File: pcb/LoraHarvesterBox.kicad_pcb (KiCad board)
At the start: 4 copper layers, 48 x 45.5 mm, 45 parts, among them J1 Conn_01x02_Pin, J2 Conn_01x02_Pin, J3 Conn_01x02_Pin, J4 Conn_01x04_Socket, J5 Conn_01x04_Socket, J6 Conn_01x04_Socket, J7 Conn_01x04_Socket, J8 Conn_01x06_Socket, J9 Conn_01x08_Socket, SW1 SSSS811101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

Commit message: docs, pcb, sch: add missing buffer capacitor to power switch
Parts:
- added C6: 1uF, Capacitor_SMD:C_0603_1608Metric_Pad1.08x0.95mm_HandSolder, F.Cu at (116.5, 88.1)
- moved J3 1.04 mm to (120.3, 88.7), turned to 0 degrees
- moved U4 0.82 mm to (116.5, 85.1), turned to 90 degrees
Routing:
- net Net-(BT1-+): track 17.5 -> 23.7 mm
- net GND: track 59.8 -> 62.4 mm, vias 176 -> 169
- net /Vdd_Input: track 3.29 -> 5.44 mm
- net +3V0: track 14.8 -> 16.7 mm, vias 10 -> 9
- net /VBAT: track 17.3 -> 16.7 mm
- net /VBAT_OK: track 36.5 -> 37.0 mm
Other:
- board text added: "v0.0.6"
- board text removed: "v0.0.5"

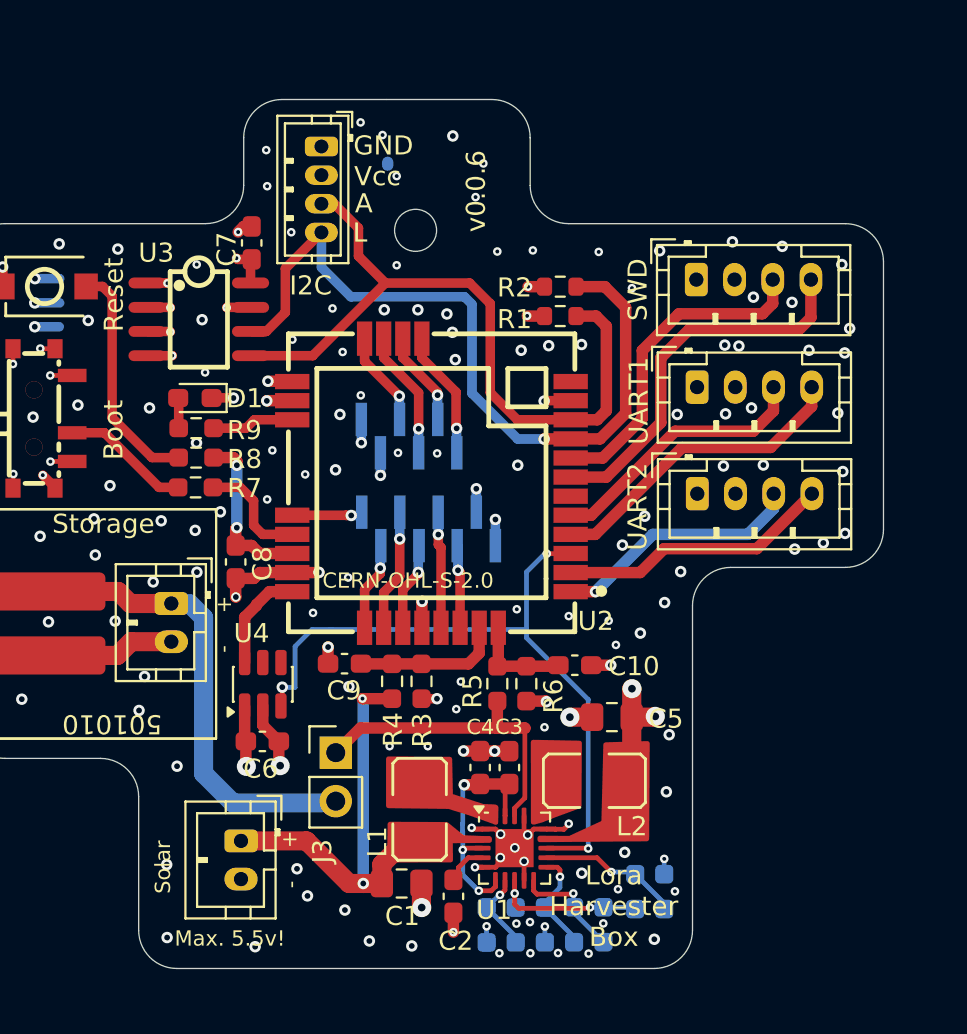
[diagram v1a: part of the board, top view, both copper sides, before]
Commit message: pcb, sch: load switch now controls the entire 3.3V rail
In the last version only the ST microcontroller was switched/on off by
the load switch. This caused problems with the periphery: they stayed
online with slowly fading into a brown out. This also fixes battery
drain by half-dead sensors.
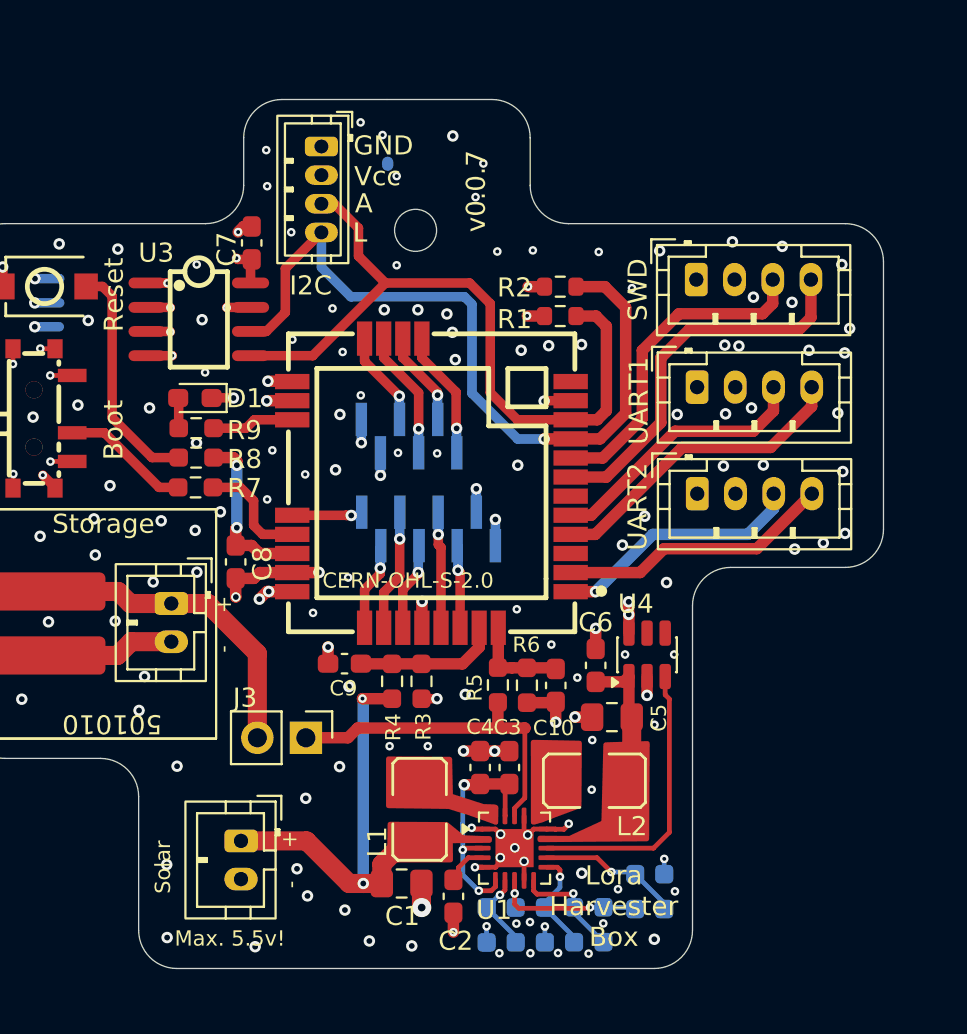
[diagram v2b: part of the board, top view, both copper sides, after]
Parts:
- moved U4 20.2 mm to (136.6, 83.6)
- moved C6 17.9 mm to (133.9, 84.1), turned to -90 degrees
- moved J3 1.75 mm to (118.8, 87.9), turned to -90 degrees
- moved C10 1.46 mm to (131.8, 85.2), turned to 90 degrees
- moved R6 0.09 mm to (130.3, 85.2)
- moved R5 0.08 mm to (128.8, 85.2)
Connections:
- C5 pad 2: +3V0 -> /VHARVESTER
- C6 pad 2: +3V0 -> /VHARVESTER
- L2 pad 2: +3V0 -> /VHARVESTER
- U1 pad 14: +3V0 -> /VHARVESTER
- U2 pad 24: /Vdd_Input -> +3V0
- U2 pad 3: /VBAT_OK -> unconnected-(U2-PA15/PIN_A4-Pad3)
- U4 pad 1: +3V0 -> /VHARVESTER
- U4 pad 6: /Vdd_Input -> +3V0
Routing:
- net /VBAT_OK: track 37.0 -> 15.0 mm, vias 3 -> 0
- net /VHARVESTER: track 0.00 -> 7.48 mm
- net Net-(BT1-+): track 23.7 -> 16.7 mm
- net +3V0: track 16.7 -> 10.9 mm, vias 9 -> 10
- net /Vdd_Input: track 5.44 -> 0.00 mm
- net /VBAT: track 16.7 -> 17.9 mm
- net GND: track 62.4 -> 61.5 mm, vias 169 -> 168
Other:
- board text added: "v0.0.7"
- board text removed: "v0.0.6"

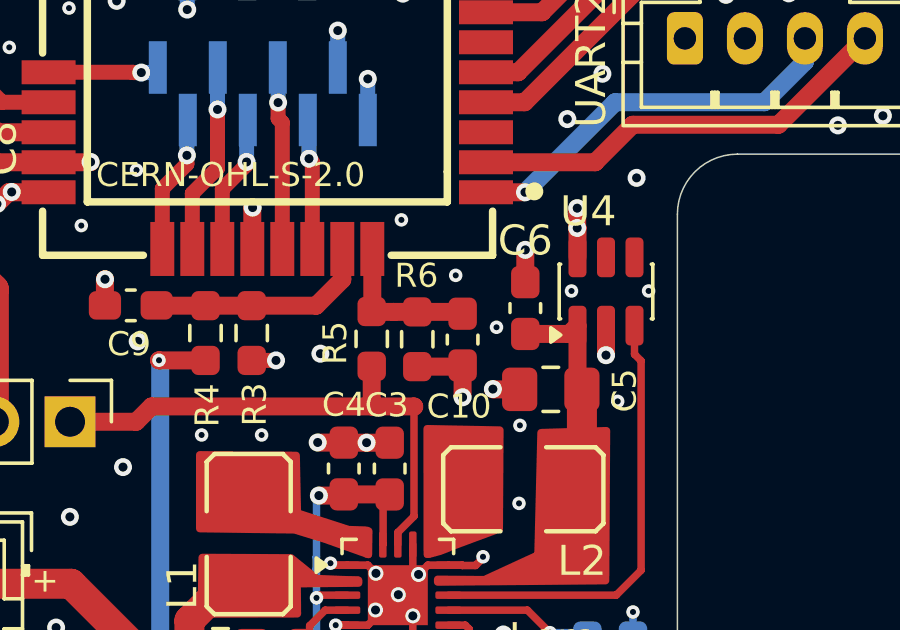
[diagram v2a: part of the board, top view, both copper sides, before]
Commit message: pcb: clean up silk prints
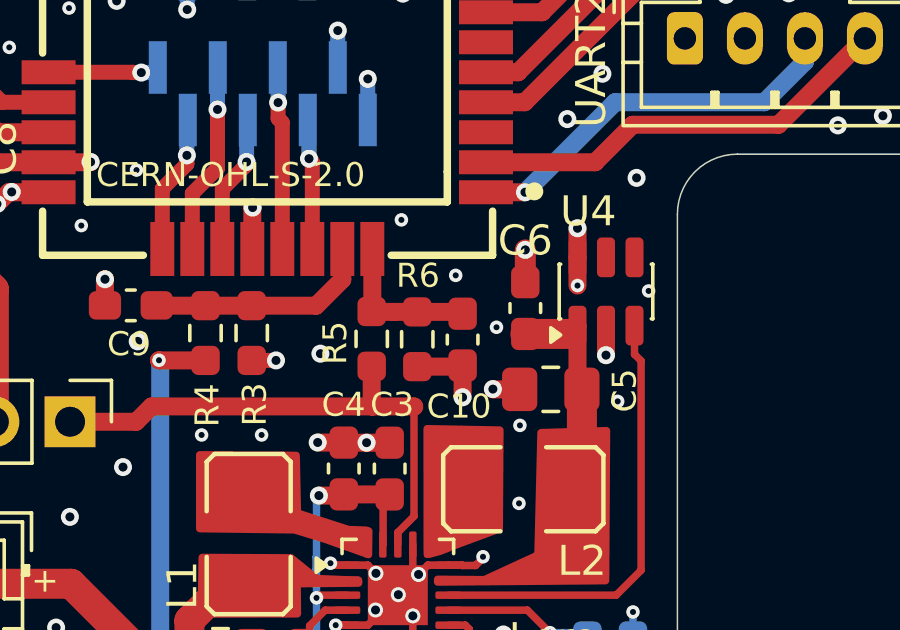
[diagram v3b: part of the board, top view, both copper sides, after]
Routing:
- net GND: vias 168 -> 167
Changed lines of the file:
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@@
 		(tags "capacitor handsolder")
 		(property "Reference" "C4"
-			(at 2.1275 0 180)
+			(at 2.1275 -0.01 180)
 			(layer "F.SilkS")
 			(effects
@@
 		(tags "capacitor handsolder")
 		(property "Reference" "C3"
-			(at 2.11 -0.1 180)
+			(at 2.13 0.08 180)
 			(layer "F.SilkS")
 			(effects
@@
 		(tags "resistor handsolder")
 		(property "Reference" "R6"
-			(at -2.12 0.03 180)
+			(at -2.12 -0.02 180)
 			(layer "F.SilkS")
 			(effects
@@
 		(start 133.93 83.2675)
 		(end 133.93 82.19)
-		(width 0.6)
+		(width 0.7)
 		(layer "F.Cu")
 		(net 2)
@@
 	)
 	(via
-		(at 135.47 83.56)
-		(size 0.45)
-		(drill 0.2)
-		(layers "F.Cu" "B.Cu")
-		(free yes)
-		(net 2)
-	)
-	(via
 		(at 134.33 97.64)
 		(size 0.45)
@@
 	)
 	(segment
-		(start 135.66 81.46)
-		(end 135.66 80.8)
-		(width 0.6)
-		(layer "F.Cu")
-		(net 3)
-	)
-	(segment
 		(start 115.92 62.8725)
 		(end 115.1825 62.8725)
@@
 	)
 	(segment
-		(start 135.67 82.44)
-		(end 135.67 81.47)
+		(start 116.81 80.26)
+		(end 116.72 80.26)
 		(width 0.6)
 		(layer "F.Cu")
@@
 	)
 	(segment
-		(start 116.81 80.26)
-		(end 116.72 80.26)
+		(start 135.67 83.38)
+		(end 135.67 82.44)
 		(width 0.6)
 		(layer "F.Cu")
@@
 	(segment
 		(start 135.67 81.47)
-		(end 135.66 81.46)
+		(end 135.67 82.44)
 		(width 0.6)
 		(layer "F.Cu")
@@
 	)
 	(via
-		(at 116.81 80.26)
-		(size 0.6)
-		(drill 0.3)
+		(at 135.67 83.38)
+		(size 0.45)
+		(drill 0.2)
 		(layers "F.Cu" "B.Cu")
 		(net 3)
 	)
 	(via
-		(at 135.66 80.8)
+		(at 116.81 80.26)
 		(size 0.6)
 		(drill 0.3)
@@
 	)
 	(via
-		(at 135.66 81.46)
+		(at 135.67 81.47)
 		(size 0.6)
 		(drill 0.3)
@@
 		(start 133.93 84.9925)
 		(end 135.3925 84.9925)
-		(width 0.6)
+		(width 1)
 		(layer "F.Cu")
 		(net 44)
